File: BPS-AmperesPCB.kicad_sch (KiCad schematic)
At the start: 44 parts, among them IC1 1769205241, IC2 TLV70130DBVR, J1 Conn_01x04, J2 PeripheralCANConnector, J3 PeripheralCANConnector, U2 INA145UA/2K5, U3 AMC1300BDWV

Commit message: finished? power on sch
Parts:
- removed C1, C3: 1uF, Capacitor_SMD:C_0805_2012Metric, symbol Device:C
- removed D5: PowerOn, LED_SMD:LED_0805_2012Metric, symbol Device:LED
- removed R10: 1.5k, Resistor_SMD:R_0805_2012Metric, symbol Device:R
- added C19, C20: 100nF, Capacitor_SMD:C_0805_2012Metric, symbol Device:C
- added D7: 3V3, LED_SMD:LED_0805_2012Metric, symbol Device:LED
- added IC3: 1769205241, Parts:1769205241, symbol WE_1769205241:1769205241
- added IC4: TLV70130DBVR, UTSVT_Power:TLV70130DBVR, symbol utsvt-power:TLV70130DBVR
- added R12: 1.5k, Resistor_SMD:R_0805_2012Metric, symbol Device:R
- C4, C5: footprint (none) -> Capacitor_SMD:C_0805_2012Metric
- D4: value PowerOn -> 12V
- D6: value PowerOn -> 3V3 High
- IC1: footprint 1769205241 -> Parts:1769205241
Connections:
- net +12V: now also R9.1, IC3.2 (+VIN)
- net +3V3: now also C20.1, IC4.1 (OUT), R12.1; no longer R11.1
- net +3V3 High: now also R11.1
- net +5V: now also C19.1, IC3.5 (+VOUT), IC4.3 (IN); no longer C4.1, IC1.5 (+VOUT), IC2.3 (IN), R9.1
- net GND: now also C19.2, C20.2, D7.1 (K), IC3.4 (-VOUT), IC4.2 (GND); no longer D6.1 (K)
- net GND High: now also D6.1 (K); no longer D4.1 (K)
- net GNDPWR: now also D4.1 (K), IC3.1 (-VIN)
- net MCU/CAN_HIGH renamed CAN_HIGH
- net MCU/CAN_LOW renamed CAN_LOW
- new net: D7.2 (A), R12.2
- new net +5V High: C4.1, IC1.5 (+VOUT), IC2.3 (IN)
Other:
- sheet Peripherals renamed MCU
- added sheet CAN (CAN.kicad_sch)
- sheet MCU: file Peripherals.kicad_sch -> MCU.kicad_sch
- sheet MCU ports: added CAN_RX, CAN_TX; removed CAN_HIGH, CAN_LOW
- note added: "Input"
- note added: "Isolated"
- note added: "Non-Isolated"
- moved on the sheet: +12V1, +3V3, +3V3H1, C4, C5, D4, D6, GND1, GNDH1, GNDPWR1, IC1, IC2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

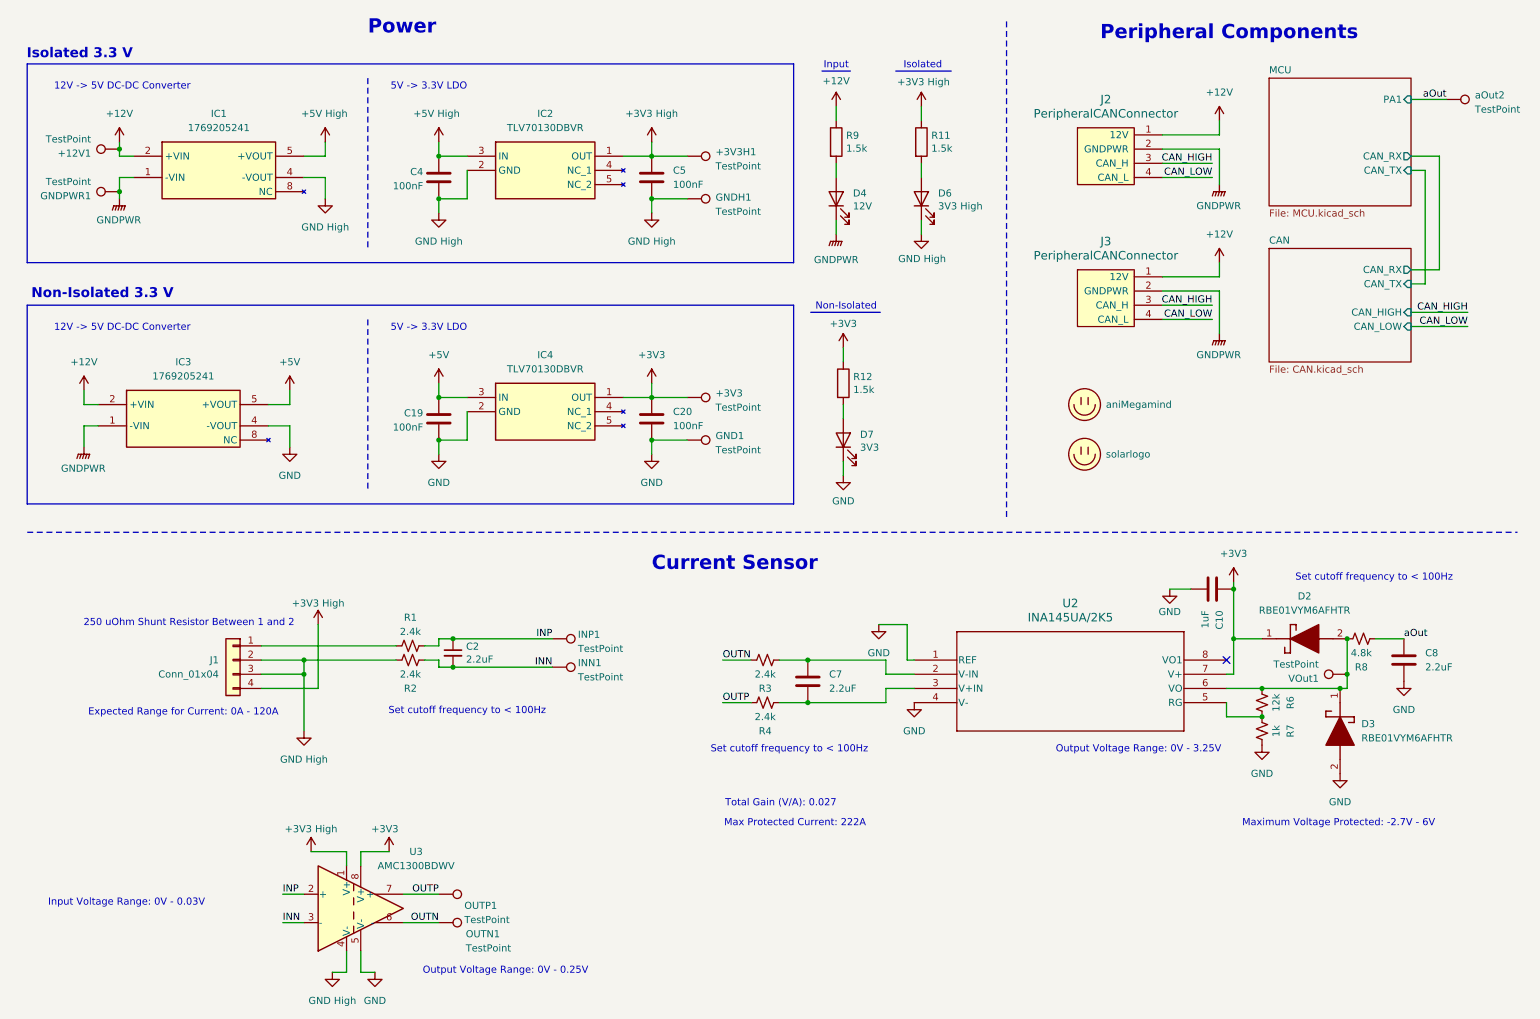
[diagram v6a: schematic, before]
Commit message: added MX cube pinout screenshot
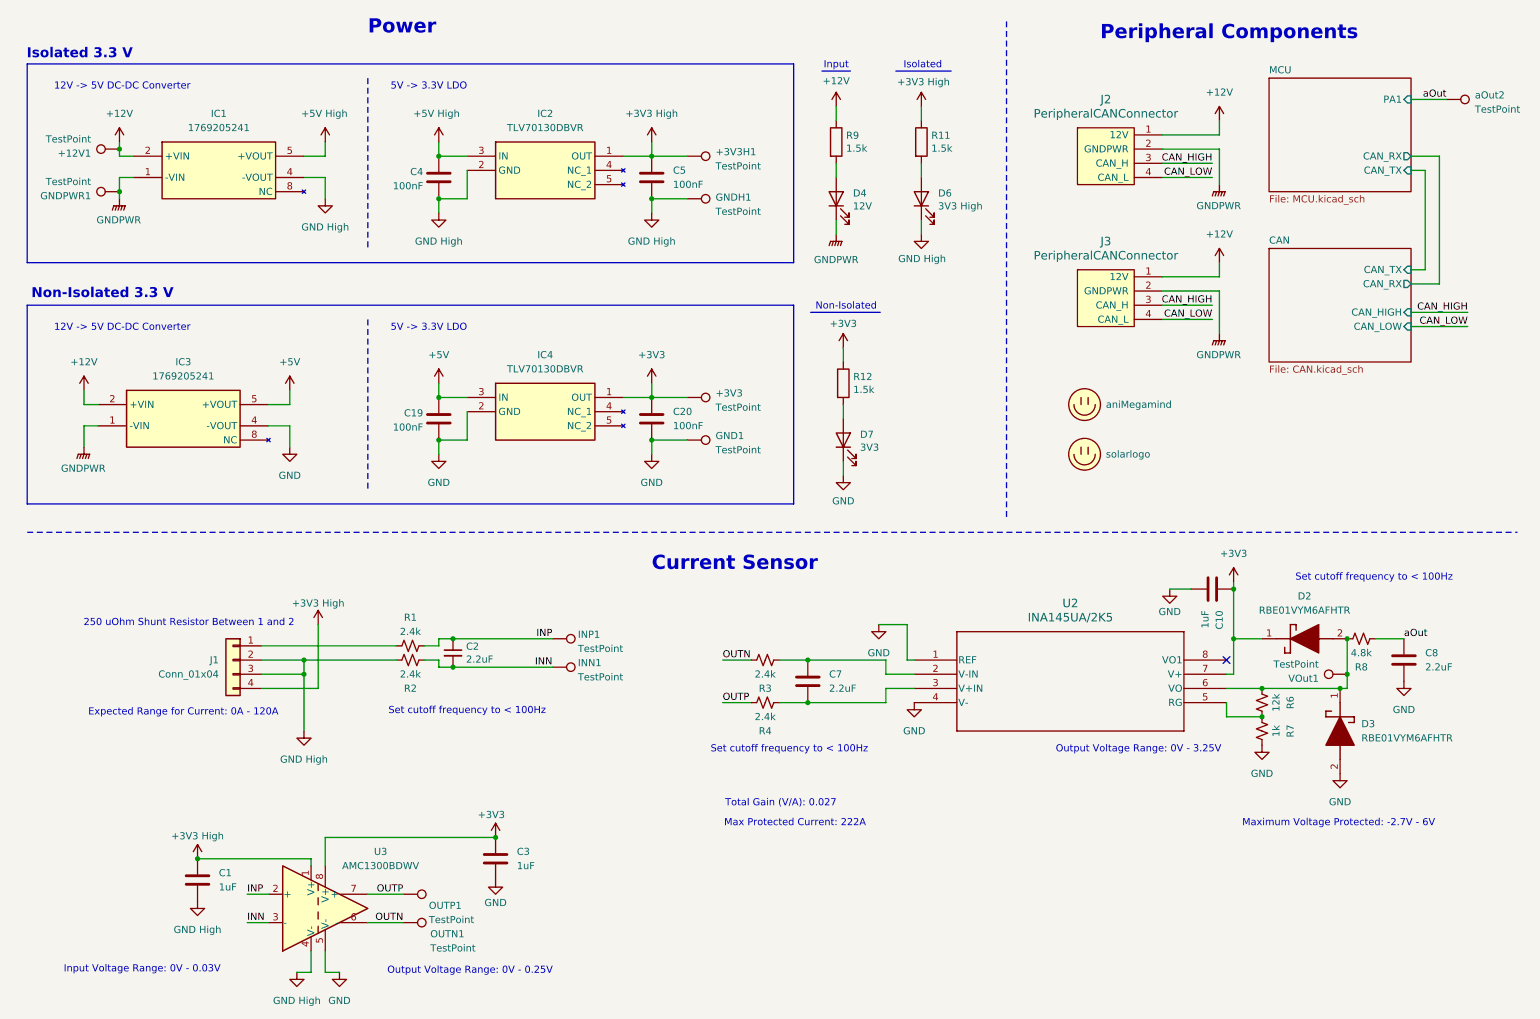
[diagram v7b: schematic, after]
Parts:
- added C1, C3: 1uF, Capacitor_SMD:C_0805_2012Metric, symbol Device:C
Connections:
- net +3V3: now also C3.1
- net +3V3 High: now also C1.1
- net GND: now also C3.2
- net GND High: now also C1.2
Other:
- moved on the sheet: OUTN1, OUTP1, U3

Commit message: power
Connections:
- net +3V3 renamed +3.3V
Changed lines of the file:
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@@
 	)
 	(junction
-		(at 99.06 161.29)
-		(diameter 0)
-		(color 0 0 0 0)
-	)
-	(junction
 		(at 127 82.55)
 		(diameter 0)
@@
 	)
 	(junction
+		(at 99.06 161.29)
+		(diameter 0)
+		(color 0 0 0 0)
+	)
+	(junction
 		(at 231.14 125.73)
 		(diameter 0)
@@
 	)
 	(symbol
-		(lib_id "power:+3V3")
-		(at 127 80.01 0)
+		(lib_id "power:+3.3V")
+		(at 161.29 73.66 0)
 		(unit 1)
 		(exclude_from_sim no)
@@
 		(on_board yes)
 		(dnp no)
-		(fields_autoplaced yes)
 		(property "Reference" "#PWR064"
-			(at 127 83.82 0)
+			(at 161.29 77.47 0)
 			(effects
 				(font
@@
 			)
 		)
-		(property "Value" "+3V3"
-			(at 127 74.93 0)
+		(property "Value" "+3.3V"
+			(at 161.29 69.596 0)
 			(effects
 				(font
@@
 		)
 		(property "Footprint" ""
-			(at 127 80.01 0)
+			(at 161.29 73.66 0)
 			(effects
 				(font
@@
 		)
 		(property "Datasheet" ""
-			(at 127 80.01 0)
+			(at 161.29 73.66 0)
 			(effects
 				(font
@@
 			)
 		)
-		(property "Description" "Power symbol creates a global label with name \"+3V3\""
-			(at 127 80.01 0)
+		(property "Description" "Power symbol creates a global label with name \"+3.3V\""
+			(at 161.29 73.66 0)
 			(effects
 				(font
@@
 		)
 		(instances
-			(project ""
+			(project "BPS-AmperesPCB"
 				(path "/a452d214-ea00-440d-a445-5d6103fda43a"
 					(reference "#PWR064")
@@
 	)
 	(symbol
-		(lib_id "power:+3V3")
-		(at 99.06 161.29 0)
-		(unit 1)
-		(exclude_from_sim no)
-		(in_bom yes)
-		(on_board yes)
-		(dnp no)
-		(property "Reference" "#PWR08"
-			(at 99.06 165.1 0)
-			(effects
-				(font
-					(size 1.27 1.27)
-				)
-				(hide yes)
-			)
-		)
-		(property "Value" "+3V3"
-			(at 98.298 157.226 0)
-			(effects
-				(font
-					(size 1.27 1.27)
-				)
-			)
-		)
-		(property "Footprint" ""
-			(at 99.06 161.29 0)
-			(effects
-				(font
-					(size 1.27 1.27)
-				)
-				(hide yes)
-			)
-		)
-		(property "Datasheet" ""
-			(at 99.06 161.29 0)
-			(effects
-				(font
-					(size 1.27 1.27)
-				)
-				(hide yes)
-			)
-		)
-		(property "Description" "Power symbol creates a global label with name \"+3V3\""
-			(at 99.06 161.29 0)
-			(effects
-				(font
-					(size 1.27 1.27)
-				)
-				(hide yes)
-			)
-		)
-		(pin "1"
-		)
-		(instances
-			(project "BPS-AmperesPCB"
-				(path "/a452d214-ea00-440d-a445-5d6103fda43a"
-					(reference "#PWR08")
-					(unit 1)
-				)
-			)
-		)
-	)
-	(symbol
 		(lib_id "utsvt-misc:Logo_Placeholder")
 		(at 204.47 83.82 0)
@@
 	)
 	(symbol
-		(lib_id "power:+3V3")
-		(at 161.29 73.66 0)
-		(unit 1)
-		(exclude_from_sim no)
-		(in_bom yes)
-		(on_board yes)
-		(dnp no)
-		(property "Reference" "#PWR055"
-			(at 161.29 77.47 0)
-			(effects
-				(font
-					(size 1.27 1.27)
-				)
-				(hide yes)
-			)
-		)
-		(property "Value" "+3V3"
-			(at 161.29 69.342 0)
-			(effects
-				(font
-					(size 1.27 1.27)
-				)
-			)
-		)
-		(property "Footprint" ""
-			(at 161.29 73.66 0)
-			(effects
-				(font
-					(size 1.27 1.27)
-				)
-				(hide yes)
-			)
-		)
-		(property "Datasheet" ""
-			(at 161.29 73.66 0)
-			(effects
-				(font
-					(size 1.27 1.27)
-				)
-				(hide yes)
-			)
-		)
-		(property "Description" "Power symbol creates a global label with name \"+3V3\""
-			(at 161.29 73.66 0)
-			(effects
-				(font
-					(size 1.27 1.27)
-				)
-				(hide yes)
-			)
-		)
-		(pin "1"
-		)
-		(instances
-			(project ""
-				(path "/a452d214-ea00-440d-a445-5d6103fda43a"
-					(reference "#PWR055")
-					(unit 1)
-				)
-			)
-		)
-	)
-	(symbol
 		(lib_id "Device:C")
 		(at 154.94 133.35 0)
@@
 	)
 	(symbol
+		(lib_id "power:+3.3V")
+		(at 127 80.01 0)
+		(unit 1)
+		(exclude_from_sim no)
+		(in_bom yes)
+		(on_board yes)
+		(dnp no)
+		(fields_autoplaced yes)
+		(property "Reference" "#PWR07"
+			(at 127 83.82 0)
+			(effects
+				(font
+					(size 1.27 1.27)
+				)
+				(hide yes)
+			)
+		)
+		(property "Value" "+3.3V"
+			(at 127 74.93 0)
+			(effects
+				(font
+					(size 1.27 1.27)
+				)
+			)
+		)
+		(property "Footprint" ""
+			(at 127 80.01 0)
+			(effects
+				(font
+					(size 1.27 1.27)
+				)
+				(hide yes)
+			)
+		)
+		(property "Datasheet" ""
+			(at 127 80.01 0)
+			(effects
+				(font
+					(size 1.27 1.27)
+				)
+				(hide yes)
+			)
+		)
+		(property "Description" "Power symbol creates a global label with name \"+3.3V\""
+			(at 127 80.01 0)
+			(effects
+				(font
+					(size 1.27 1.27)
+				)
+				(hide yes)
+			)
+		)
+		(pin "1"
+		)
+		(instances
+			(project ""
+				(path "/a452d214-ea00-440d-a445-5d6103fda43a"
+					(reference "#PWR07")
+					(unit 1)
+				)
+			)
+		)
+	)
+	(symbol
 		(lib_id "Device:C")
 		(at 99.06 165.1 0)
@@
 	)
 	(symbol
+		(lib_id "power:+3.3V")
+		(at 231.14 115.57 0)
+		(unit 1)
+		(exclude_from_sim no)
+		(in_bom yes)
+		(on_board yes)
+		(dnp no)
+		(fields_autoplaced yes)
+		(property "Reference" "#PWR08"
+			(at 231.14 119.38 0)
+			(effects
+				(font
+					(size 1.27 1.27)
+				)
+				(hide yes)
+			)
+		)
+		(property "Value" "+3.3V"
+			(at 231.14 110.49 0)
+			(effects
+				(font
+					(size 1.27 1.27)
+				)
+			)
+		)
+		(property "Footprint" ""
+			(at 231.14 115.57 0)
+			(effects
+				(font
+					(size 1.27 1.27)
+				)
+				(hide yes)
+			)
+		)
+		(property "Datasheet" ""
+			(at 231.14 115.57 0)
+			(effects
+				(font
+					(size 1.27 1.27)
+				)
+				(hide yes)
+			)
+		)
+		(property "Description" "Power symbol creates a global label with name \"+3.3V\""
+			(at 231.14 115.57 0)
+			(effects
+				(font
+					(size 1.27 1.27)
+				)
+				(hide yes)
+			)
+		)
+		(pin "1"
+		)
+		(instances
+			(project "BPS-AmperesPCB"
+				(path "/a452d214-ea00-440d-a445-5d6103fda43a"
+					(reference "#PWR08")
+					(unit 1)
+				)
+			)
+		)
+	)
+	(symbol
 		(lib_id "INA145:INA145UA_2K5")
 		(at 173.99 129.54 0)
@@
 	)
 	(symbol
-		(lib_id "power:+3V3")
-		(at 231.14 115.57 0)
+		(lib_id "power:+3.3V")
+		(at 99.06 161.29 0)
 		(unit 1)
 		(exclude_from_sim no)
@@
 		(dnp no)
 		(fields_autoplaced yes)
-		(property "Reference" "#PWR021"
-			(at 231.14 119.38 0)
+		(property "Reference" "#PWR055"
+			(at 99.06 165.1 0)
 			(effects
 				(font
@@
 			)
 		)
-		(property "Value" "+3V3"
-			(at 231.14 110.49 0)
+		(property "Value" "+3.3V"
+			(at 99.06 156.21 0)
 			(effects
 				(font
@@
 		)
 		(property "Footprint" ""
-			(at 231.14 115.57 0)
+			(at 99.06 161.29 0)
 			(effects
 				(font
@@
 		)
 		(property "Datasheet" ""
-			(at 231.14 115.57 0)
+			(at 99.06 161.29 0)
 			(effects
 				(font
@@
 			)
 		)
-		(property "Description" "Power symbol creates a global label with name \"+3V3\""
-			(at 231.14 115.57 0)
+		(property "Description" "Power symbol creates a global label with name \"+3.3V\""
+			(at 99.06 161.29 0)
 			(effects
 				(font
@@
 			(project "BPS-AmperesPCB"
 				(path "/a452d214-ea00-440d-a445-5d6103fda43a"
-					(reference "#PWR021")
+					(reference "#PWR055")
 					(unit 1)
 				)
